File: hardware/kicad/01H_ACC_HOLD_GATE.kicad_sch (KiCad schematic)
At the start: 20 parts, among them Q912 MMBT5551, Q913 MMBT5551, Q914 PMBT5551,215, Q915 MMBT5401-7-F, U911 140356145000 HOLD

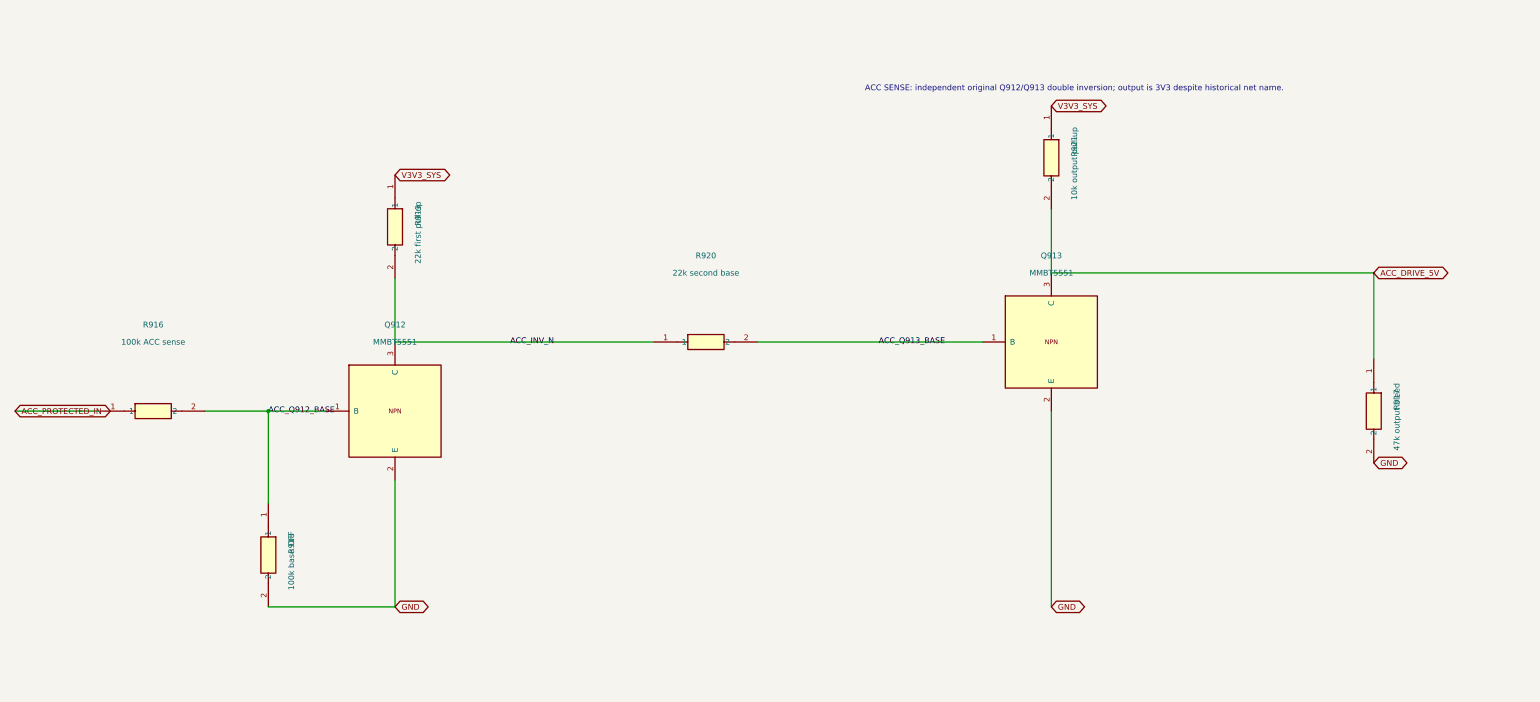
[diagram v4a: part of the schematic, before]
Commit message: fix(power): prearm timed HOLD before ACC falls and protect inverse-ACC sensing
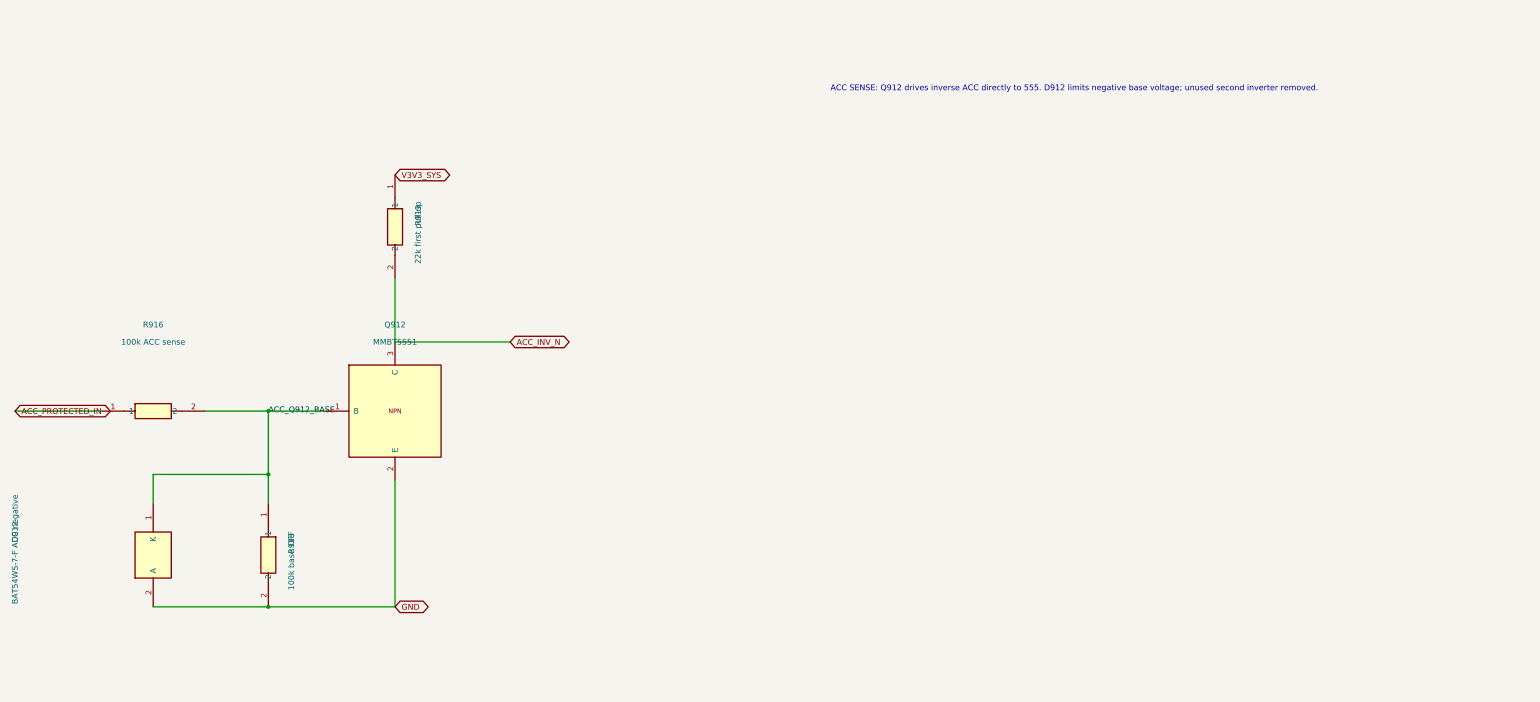
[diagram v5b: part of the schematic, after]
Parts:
- removed Q913: MMBT5551, Tripmaster:Q_SOT23_1B2E3C, symbol TripTracer_V1:MMBT5551
- removed R917: 47k output bleed, Tripmaster:R_1206_3216, symbol Tripmaster_Sym:R
- removed R920: 22k second base, Tripmaster:R_1206_3216, symbol Tripmaster_Sym:R
- removed R921: 10k output pull-up, Tripmaster:R_1206_3216, symbol Tripmaster_Sym:R
- added D912: BAT54WS-7-F ACC negative, Diode_SMD:D_SOD-323, symbol TripTracer_V1:BAT54WS_CLAMP
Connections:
- net ACC_Q912_BASE: now also D912.1 (K)
- net GND: now also D912.2 (A)
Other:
- note added: "ACC SENSE: Q912 drives inverse ACC directly to 555. D912 limits negative base voltage; unused second inverter removed."
- note removed: "ACC SENSE: independent original Q912/Q913 double inversion; output is 3V3 despite historical net name."
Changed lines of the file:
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@@
 (wire (pts (xy 444.5 115.57) (xy 515.62 115.57)) (stroke (width 0) (type default)))
 (global_label "BUCK_ENABLE" (shape bidirectional) (at 515.62 115.57 0) (effects (font (size 1.27 1.27)) (justify left)))
-(text "ACC SENSE: independent original Q912/Q913 double inversion; output is 3V3 despite historical net name." (at 264.16 205.74 0) (effects (font (size 1.27 1.27))))
+(text "ACC SENSE: Q912 drives inverse ACC directly to 555. D912 limits negative base voltage; unused second inverter removed." (at 264.16 205.74 0) (effects (font (size 1.27 1.27))))
 (symbol (lib_id "Tripmaster_Sym:R") (at 60.96 276.86 0) (unit 1) (in_bom yes) (on_board yes) (dnp no)
 (property "Reference" "R916" (at 60.96 257.81 0) (effects (font (size 1.27 1.27))))
@@
 (pin "2")
 (instances (project "TripTracer_V1" (path "/a26d9b0c-7f10-4e5a-a65f-000000000064/a26d9b0c-7f10-4e5a-a65f-000000000065" (reference "R919") (unit 1)))))
-(symbol (lib_id "Tripmaster_Sym:R") (at 182.88 261.62 0) (unit 1) (in_bom yes) (on_board yes) (dnp no)
-(property "Reference" "R920" (at 182.88 242.57 0) (effects (font (size 1.27 1.27))))
-(property "Value" "22k second base" (at 182.88 246.38 0) (effects (font (size 1.27 1.27))))
-(property "Footprint" "Tripmaster:R_1206_3216" (at 182.88 261.62 0) (effects (font (size 1.27 1.27)) (hide yes)))
-(pin "1")
-(pin "2")
-(instances (project "TripTracer_V1" (path "/a26d9b0c-7f10-4e5a-a65f-000000000064/a26d9b0c-7f10-4e5a-a65f-000000000065" (reference "R920") (unit 1)))))
-(symbol (lib_id "TripTracer_V1:MMBT5551") (at 259.08 261.62 0) (unit 1) (in_bom yes) (on_board yes) (dnp no)
-(property "Reference" "Q913" (at 259.08 242.57 0) (effects (font (size 1.27 1.27))))
-(property "Value" "MMBT5551" (at 259.08 246.38 0) (effects (font (size 1.27 1.27))))
-(property "Footprint" "Tripmaster:Q_SOT23_1B2E3C" (at 259.08 261.62 0) (effects (font (size 1.27 1.27)) (hide yes)))
-(pin "1")
-(pin "2")
-(pin "3")
-(instances (project "TripTracer_V1" (path "/a26d9b0c-7f10-4e5a-a65f-000000000064/a26d9b0c-7f10-4e5a-a65f-000000000065" (reference "Q913") (unit 1)))))
-(symbol (lib_id "Tripmaster_Sym:R") (at 259.08 220.98 270) (unit 1) (in_bom yes) (on_board yes) (dnp no)
-(property "Reference" "R921" (at 264.16 218.44 0) (effects (font (size 1.27 1.27))))
-(property "Value" "10k output pull-up" (at 264.16 222.25 0) (effects (font (size 1.27 1.27))))
-(property "Footprint" "Tripmaster:R_1206_3216" (at 259.08 220.98 0) (effects (font (size 1.27 1.27)) (hide yes)))
-(pin "1")
-(pin "2")
-(instances (project "TripTracer_V1" (path "/a26d9b0c-7f10-4e5a-a65f-000000000064/a26d9b0c-7f10-4e5a-a65f-000000000065" (reference "R921") (unit 1)))))
-(symbol (lib_id "Tripmaster_Sym:R") (at 330.2 276.86 270) (unit 1) (in_bom yes) (on_board yes) (dnp no)
-(property "Reference" "R917" (at 335.28 274.32 0) (effects (font (size 1.27 1.27))))
-(property "Value" "47k output bleed" (at 335.28 278.13 0) (effects (font (size 1.27 1.27))))
-(property "Footprint" "Tripmaster:R_1206_3216" (at 330.2 276.86 0) (effects (font (size 1.27 1.27)) (hide yes)))
-(pin "1")
-(pin "2")
-(instances (project "TripTracer_V1" (path "/a26d9b0c-7f10-4e5a-a65f-000000000064/a26d9b0c-7f10-4e5a-a65f-000000000065" (reference "R917") (unit 1)))))
 (global_label "ACC_PROTECTED_IN" (shape bidirectional) (at 30.48 276.86 0) (effects (font (size 1.27 1.27)) (justify left)))
 (wire (pts (xy 30.48 276.86) (xy 49.53 276.86)) (stroke (width 0) (type default)))
@@
 (global_label "V3V3_SYS" (shape bidirectional) (at 114.3 224.79 0) (effects (font (size 1.27 1.27)) (justify left)))
 (wire (pts (xy 114.3 247.65) (xy 114.3 261.62)) (stroke (width 0) (type default)))
-(wire (pts (xy 114.3 261.62) (xy 171.45 261.62)) (stroke (width 0) (type default)))
-(label "ACC_INV_N" (at 139.7 261.62 0) (effects (font (size 1.27 1.27))))
-(wire (pts (xy 194.31 261.62) (xy 243.84 261.62)) (stroke (width 0) (type default)))
-(label "ACC_Q913_BASE" (at 220.98 261.62 0) (effects (font (size 1.27 1.27))))
-(global_label "V3V3_SYS" (shape bidirectional) (at 259.08 209.55 0) (effects (font (size 1.27 1.27)) (justify left)))
-(wire (pts (xy 259.08 232.41) (xy 259.08 246.38)) (stroke (width 0) (type default)))
-(wire (pts (xy 259.08 246.38) (xy 330.2 246.38)) (stroke (width 0) (type default)))
-(wire (pts (xy 330.2 246.38) (xy 330.2 265.43)) (stroke (width 0) (type default)))
-(global_label "ACC_DRIVE_5V" (shape bidirectional) (at 330.2 246.38 0) (effects (font (size 1.27 1.27)) (justify left)))
-(global_label "GND" (shape bidirectional) (at 330.2 288.29 0) (effects (font (size 1.27 1.27)) (justify left)))
-(wire (pts (xy 259.08 276.86) (xy 259.08 320.04)) (stroke (width 0) (type default)))
-(global_label "GND" (shape bidirectional) (at 259.08 320.04 0) (effects (font (size 1.27 1.27)) (justify left)))
+(wire (pts (xy 114.3 261.62) (xy 139.7 261.62)) (stroke (width 0) (type default)))
+(global_label "ACC_INV_N" (shape bidirectional) (at 139.7 261.62 0) (effects (font (size 1.27 1.27))))
 (text "LAB ONLY: check hot leakage, timing overlap at ACC fall, VIN/EN disconnect slew, reverse inputs and vehicle pulses. No vehicle approval." (at 284.48 365.76 0) (effects (font (size 1.27 1.27))))
-(sheet_instances (path "/" (page "1"))))
+(sheet_instances (path "/" (page "1")))
+(symbol (lib_id "TripTracer_V1:BAT54WS_CLAMP") (at 60.96 308.61 90) (unit 1) (in_bom yes) (on_board yes) (dnp no)
+(property "Reference" "D912" (at 30.48 303.53 0) (effects (font (size 1.27 1.27))))
+(property "Value" "BAT54WS-7-F ACC negative" (at 30.48 307.34 0) (effects (font (size 1.27 1.27))))
+(property "Footprint" "Diode_SMD:D_SOD-323" (at 60.96 308.61 0) (effects (font (size 1.27 1.27)) (hide yes)))
+(property "MPN" "BAT54WS-7-F" (at 60.96 308.61 0) (effects (font (size 1.27 1.27)) (hide yes)))
+(pin "1")
+(pin "2")
+(instances (project "TripTracer_V1" (path "/a26d9b0c-7f10-4e5a-a65f-000000000064/a26d9b0c-7f10-4e5a-a65f-000000000065" (reference "D912") (unit 1)))))
+(wire (pts (xy 60.96 297.18) (xy 60.96 290.83)) (stroke (width 0) (type default)))
+(wire (pts (xy 60.96 290.83) (xy 86.36 290.83)) (stroke (width 0) (type default)))
+(wire (pts (xy 60.96 320.04) (xy 86.36 320.04)) (stroke (width 0) (type default)))
+(junction (at 86.36 290.83) (diameter 0) (color 0 0 0 0))
+(junction (at 86.36 320.04) (diameter 0) (color 0 0 0 0))
+)

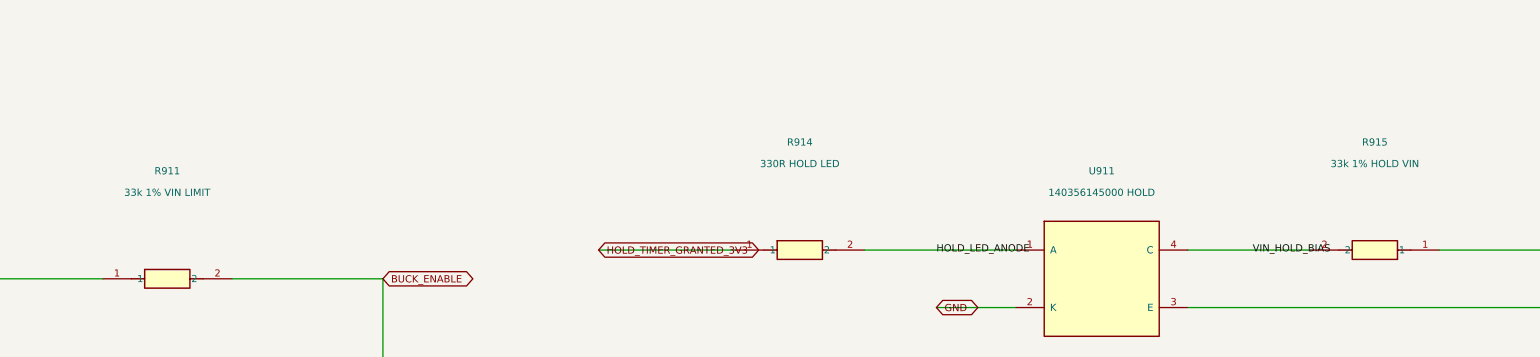
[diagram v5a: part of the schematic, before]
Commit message: Replace under-clamped input with 58V flat-clamp candidate and 1kV reverse rectifier
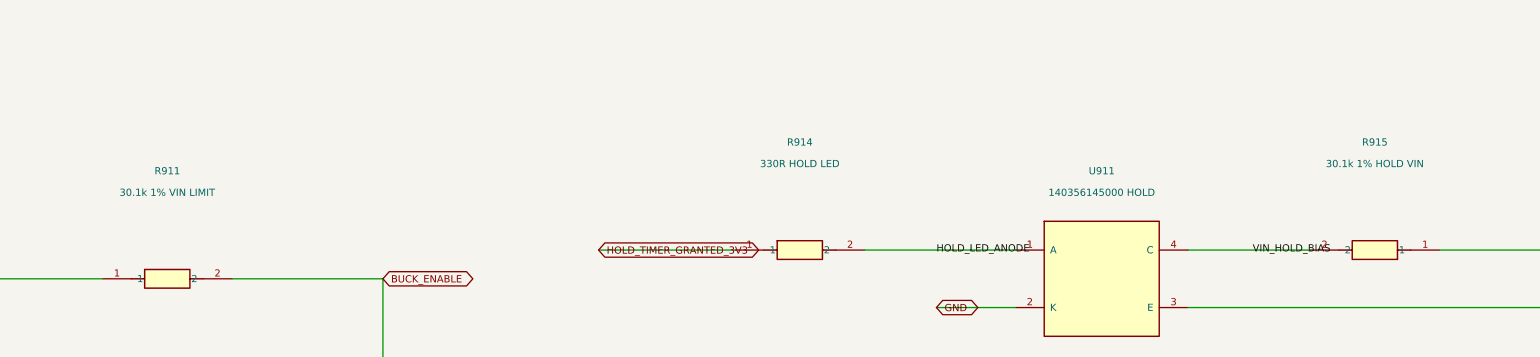
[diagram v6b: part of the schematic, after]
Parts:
- R911: value 33k 1% VIN LIMIT -> 30.1k 1% VIN LIMIT
- R915: value 33k 1% HOLD VIN -> 30.1k 1% HOLD VIN
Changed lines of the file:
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@@
 (symbol (lib_id "Tripmaster_Sym:R") (at 264.16 110.49 0) (unit 1) (in_bom yes) (on_board yes) (dnp no)
 (property "Reference" "R911" (at 264.16 91.44 0) (effects (font (size 1.27 1.27))))
-(property "Value" "33k 1% VIN LIMIT" (at 264.16 95.25 0) (effects (font (size 1.27 1.27))))
+(property "Value" "30.1k 1% VIN LIMIT" (at 264.16 95.25 0) (effects (font (size 1.27 1.27))))
 (property "Footprint" "Tripmaster:R_1206_3216" (at 264.16 110.49 0) (effects (font (size 1.27 1.27)) (hide yes)))
 (pin "1")
@@
 (symbol (lib_id "Tripmaster_Sym:R") (at 477.52 105.41 180) (unit 1) (in_bom yes) (on_board yes) (dnp no)
 (property "Reference" "R915" (at 477.52 86.36 0) (effects (font (size 1.27 1.27))))
-(property "Value" "33k 1% HOLD VIN" (at 477.52 90.17 0) (effects (font (size 1.27 1.27))))
+(property "Value" "30.1k 1% HOLD VIN" (at 477.52 90.17 0) (effects (font (size 1.27 1.27))))
 (property "Footprint" "Tripmaster:R_1206_3216" (at 477.52 105.41 0) (effects (font (size 1.27 1.27)) (hide yes)))
 (pin "1")

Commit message: Correct 9V HOLD for wiring loss and define replaceable source fuse candidates
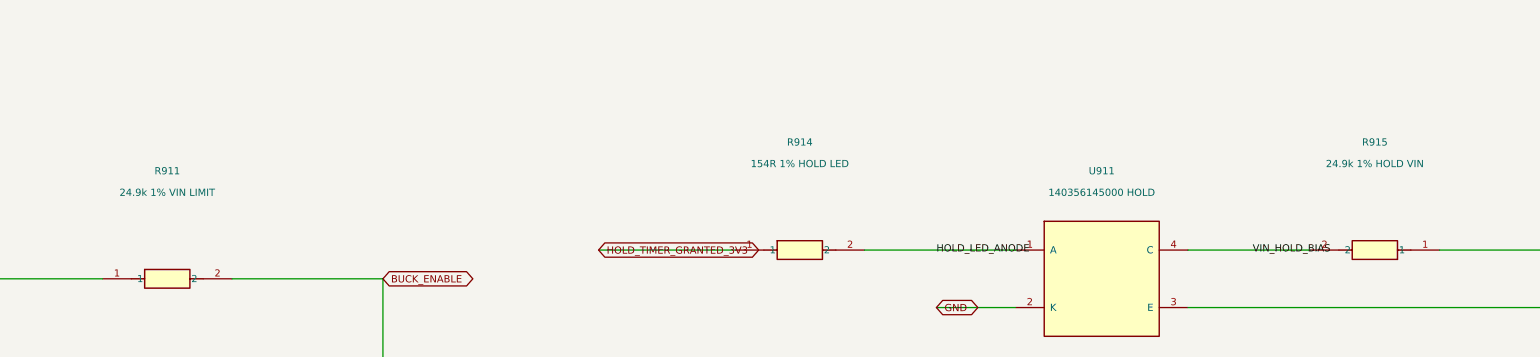
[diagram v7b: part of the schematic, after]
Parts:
- R911: value 30.1k 1% VIN LIMIT -> 24.9k 1% VIN LIMIT
- R914: value 330R HOLD LED -> 154R 1% HOLD LED
- R915: value 30.1k 1% HOLD VIN -> 24.9k 1% HOLD VIN
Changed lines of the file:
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@@
 (symbol (lib_id "Tripmaster_Sym:R") (at 264.16 110.49 0) (unit 1) (in_bom yes) (on_board yes) (dnp no)
 (property "Reference" "R911" (at 264.16 91.44 0) (effects (font (size 1.27 1.27))))
-(property "Value" "30.1k 1% VIN LIMIT" (at 264.16 95.25 0) (effects (font (size 1.27 1.27))))
+(property "Value" "24.9k 1% VIN LIMIT" (at 264.16 95.25 0) (effects (font (size 1.27 1.27))))
 (property "Footprint" "Tripmaster:R_1206_3216" (at 264.16 110.49 0) (effects (font (size 1.27 1.27)) (hide yes)))
 (pin "1")
@@
 (symbol (lib_id "Tripmaster_Sym:R") (at 375.92 105.41 0) (unit 1) (in_bom yes) (on_board yes) (dnp no)
 (property "Reference" "R914" (at 375.92 86.36 0) (effects (font (size 1.27 1.27))))
-(property "Value" "330R HOLD LED" (at 375.92 90.17 0) (effects (font (size 1.27 1.27))))
+(property "Value" "154R 1% HOLD LED" (at 375.92 90.17 0) (effects (font (size 1.27 1.27))))
 (property "Footprint" "Tripmaster:R_1206_3216" (at 375.92 105.41 0) (effects (font (size 1.27 1.27)) (hide yes)))
 (pin "1")
@@
 (symbol (lib_id "Tripmaster_Sym:R") (at 477.52 105.41 180) (unit 1) (in_bom yes) (on_board yes) (dnp no)
 (property "Reference" "R915" (at 477.52 86.36 0) (effects (font (size 1.27 1.27))))
-(property "Value" "30.1k 1% HOLD VIN" (at 477.52 90.17 0) (effects (font (size 1.27 1.27))))
+(property "Value" "24.9k 1% HOLD VIN" (at 477.52 90.17 0) (effects (font (size 1.27 1.27))))
 (property "Footprint" "Tripmaster:R_1206_3216" (at 477.52 105.41 0) (effects (font (size 1.27 1.27)) (hide yes)))
 (pin "1")
